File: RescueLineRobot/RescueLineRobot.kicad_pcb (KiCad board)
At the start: 2 copper layers, 100 x 100 mm, 8 parts, among them J1 Conn_01x11, J2 Bateria, J3 Motor 1, J4 Motor 2, J5 Convertidor, U1 ROB-14450, U2 ESP32-DEVKIT-V1

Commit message: updates
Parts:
- added J6: Laser 1, Connector_JST:JST_XH_B4B-XH-A_1x04_P2.50mm_Vertical, F.Cu at (168.0, 56.2)
- added J7: Laser 2, Connector_JST:JST_XH_B4B-XH-A_1x04_P2.50mm_Vertical, F.Cu at (168.0, 64.0)
- added J8: Laser 3, Connector_JST:JST_XH_B4B-XH-A_1x04_P2.50mm_Vertical, F.Cu at (168.0, 72.5)
- moved J4 7.52 mm to (170.0, 98.5)
- moved J3 6.77 mm to (228.8, 99.0)
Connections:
- U2 pad 11: unconnected-(U2-D21-Pad11) -> Net-(J6-Pin_4)
- U2 pad 14: unconnected-(U2-D22-Pad14) -> Net-(J6-Pin_3)
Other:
- board size 100 x 100 mm -> 80 x 100 mm

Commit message: Motores funcionan :D
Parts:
- moved U1 27.4 mm to (185.4, 90.2)
- moved J1 26.5 mm to (234.4, 70.0), turned to -90 degrees
- moved J3 17.8 mm to (219.8, 114.3)
- moved U2 15.6 mm to (215.9, 75.2)
- moved J4 9.51 mm to (168.9, 108.0)
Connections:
- U2 pad 10: Net-(U1-PWMA) -> Net-(U1-PWMB)
- U2 pad 26: Net-(U1-AI1) -> unconnected-(U2-D14-Pad26)
- U2 pad 28: Net-(U1-AI2) -> unconnected-(U2-D13-Pad28)
- U2 pad 5: Net-(U1-BI2) -> Net-(U1-PWMA)
- U2 pad 6: unconnected-(U2-RX2-Pad6) -> Net-(U1-AI2)
- U2 pad 7: unconnected-(U2-TX2-Pad7) -> Net-(U1-AI1)
- U2 pad 9: Net-(U1-PWMB) -> Net-(U1-BI2)

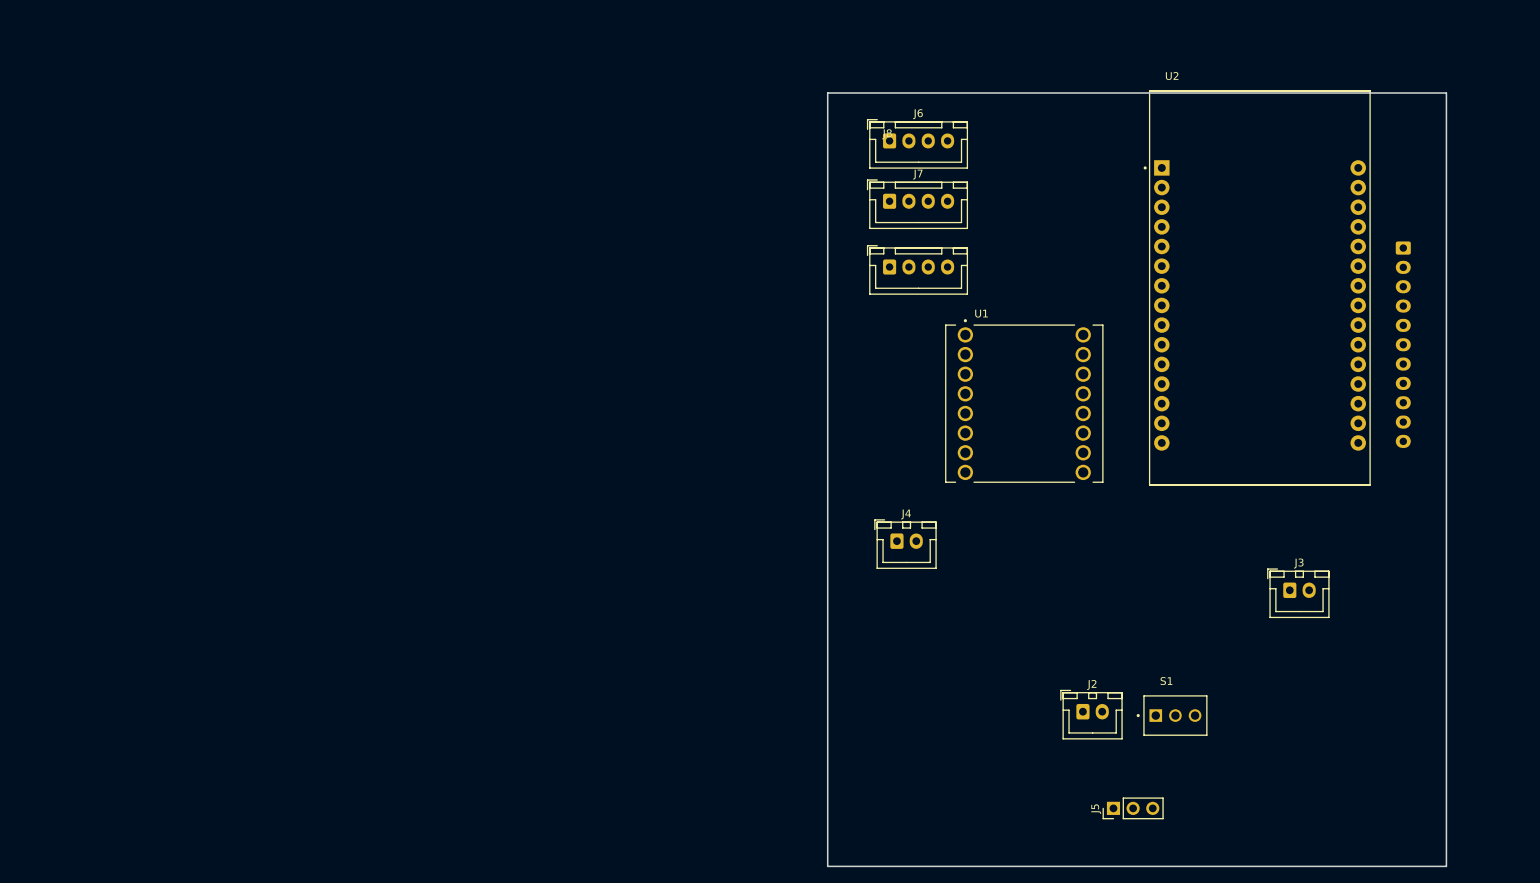
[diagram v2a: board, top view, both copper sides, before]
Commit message: Actualizacion de pcb
Ahora la pcb está más limpia y con serigrafía
Pendientes:
-2 Sensores RGB
-1 Botón pulsador
-2 Encoders para los motores (aun no se si cuadraticos o no)
-1 Puerto para servo (maybe con selector de voltaje)
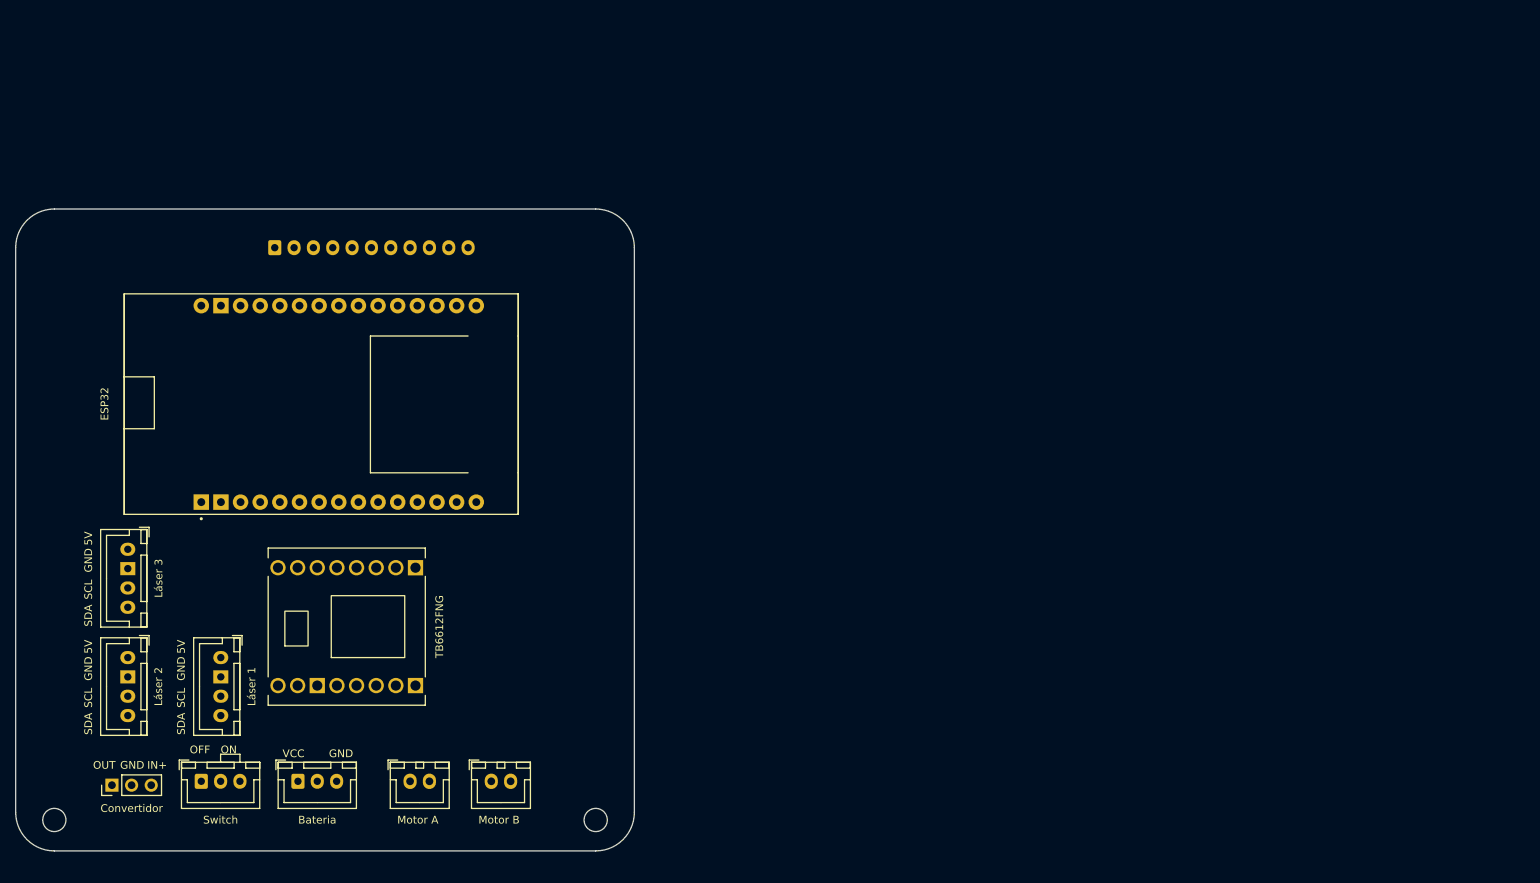
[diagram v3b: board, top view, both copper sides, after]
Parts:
- removed J2: Bateria, Connector_JST:JST_XH_B2B-XH-A_1x02_P2.50mm_Vertical
- removed J3: Motor 1, Connector_JST:JST_XH_B2B-XH-A_1x02_P2.50mm_Vertical
- removed J4: Motor 2, Connector_JST:JST_XH_B2B-XH-A_1x02_P2.50mm_Vertical
- removed J5: Convertidor, Connector_PinHeader_2.54mm:PinHeader_1x03_P2.54mm_Vertical
- removed S1: 200MSP1T2B4M2QE, 200MSP1T2B4M2QE:SW_200MSP1T2B4M2QE
- added Bateria: Bateria, Connector_JST:JST_XH_B3B-XH-A_1x03_P2.50mm_Vertical, F.Cu at (91.5, 139.0)
- added Convertidor: Convertidor, Connector_PinHeader_2.54mm:PinHeader_1x03_P2.54mm_Vertical, F.Cu at (67.5, 139.5)
- added Motor A: Motor 1, Connector_JST:JST_XH_B2B-XH-A_1x02_P2.50mm_Vertical, F.Cu at (106.0, 139.0)
- added Motor B: Motor 2, Connector_JST:JST_XH_B2B-XH-A_1x02_P2.50mm_Vertical, F.Cu at (116.5, 139.0)
- added Switch: Switch, Connector_JST:JST_XH_B3B-XH-A_1x03_P2.50mm_Vertical, F.Cu at (79.0, 139.0)
- Láser 1: renamed from J6
- Láser 2: renamed from J8
- Láser 3: renamed from J7
- moved J1 145.9 mm to (88.5, 70.0), turned to 0 degrees
- moved ESP32 122.3 mm to (94.5, 90.2), turned to 90 degrees
- moved Láser 2 110.7 mm to (69.5, 123.0), turned to -90 degrees
- moved Láser 1 109.3 mm to (81.5, 123.0), turned to -90 degrees
- moved Láser 3 108.3 mm to (69.5, 109.0), turned to -90 degrees
- moved TB6612FNG 92.2 mm to (97.8, 119.0), turned to 90 degrees
- renumbered U2 to ESP32, U1 to TB6612FNG
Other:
- board size 80 x 100 mm -> 80 x 83 mm
- board text added: "5V"
- board text added: "GND"
- board text added: "IN+"
- board text added: "OFF"
- board text added: "ON"
- board text added: "OUT"
- board text added: "SCL"
- board text added: "SDA"
- board text added: "VCC"

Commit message: Boton y encoders
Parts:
- added Boton1: SW_Push, Button_Switch_THT:SW_PUSH-12mm, F.Cu at (123.0, 124.8)
- added EncoderA1: Encoder A, Connector_JST:JST_XA_B03B-XASK-1_1x03_P2.50mm_Vertical, F.Cu at (106.0, 117.5)
- added EncoderB1: Encoder B, Connector_JST:JST_XA_B03B-XASK-1_1x03_P2.50mm_Vertical, F.Cu at (106.0, 131.5)
- added Resistencia1: R, Resistor_THT:R_Axial_DIN0617_L17.0mm_D6.0mm_P25.40mm_Horizontal, F.Cu at (106.7, 71.0)
- Laser1: renamed from Láser 1
- Laser2: renamed from Láser 3
- Laser3: renamed from Láser 2
- MotorA1: renamed from Motor A
- MotorB1: renamed from Motor B; value Motor 2 -> MotorB
- moved Laser1 30.9 mm to (69.5, 94.5)
- moved MotorA1 30.2 mm to (81.0, 122.0)
- moved MotorB1 30.2 mm to (91.5, 122.0)
- moved SigueLineas1 21.1 mm to (83.5, 49.5)
- moved Esp32 18.5 mm to (94.5, 71.7)
- moved TB6612FNG1 18.5 mm to (96.2, 100.6)
- renumbered Bateria to Bateria1, Convertidor to Convertidor1, ESP32 to Esp32, J1 to SigueLineas1, Switch to Switch1, TB6612FNG to TB6612FNG1
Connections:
- Esp32 pad 26: unconnected-(U2-D14-Pad26) -> Net-(EncoderB1-Pin_2)
- Esp32 pad 27: unconnected-(U2-D12-Pad27) -> Net-(Esp32-D12)
- Esp32 pad 28: unconnected-(U2-D13-Pad28) -> Net-(EncoderA1-Pin_2)
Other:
- board size 80 x 83 mm -> 80 x 103 mm

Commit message: Estamos Casi
Están todas las rutas hechas, todos los puertos necesarios, sólo falta nombrar al robot y poner gráficas
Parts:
- removed Convertidor1: Convertidor, Connector_PinHeader_2.54mm:PinHeader_1x03_P2.54mm_Vertical
- added Convertidor: Convertidor, Connector_PinHeader_2.54mm:PinHeader_1x03_P2.54mm_Vertical, F.Cu at (67.4, 139.0)
- added I2C1: ~, Connector_JST:JST_XH_B4B-XH-A_1x04_P2.50mm_Vertical, F.Cu at (128.3, 68.2)
- added I2C2: ~, Connector_JST:JST_XH_B4B-XH-A_1x04_P2.50mm_Vertical, F.Cu at (128.2, 53.0)
- added RGB1: ~, Connector_JST:JST_XH_B4B-XH-A_1x04_P2.50mm_Vertical, F.Cu at (128.5, 90.0)
- added RGB2: ~, Connector_JST:JST_XH_B4B-XH-A_1x04_P2.50mm_Vertical, F.Cu at (128.5, 104.6)
- added SERVO: Conn_01x03, Connector_JST:JST_XH_B3B-XH-A_1x03_P2.50mm_Vertical, F.Cu at (118.0, 106.0)
- added SERVOPOWER: Conn_01x03, Connector_PinHeader_1.27mm:PinHeader_1x03_P1.27mm_Vertical, F.Cu at (117.5, 95.2)
- EncoderA: renamed from EncoderA1; moved to B.Cu
- EncoderB: renamed from EncoderB1; moved to B.Cu
- MotorA: renamed from MotorA1; moved to B.Cu
- MotorB: renamed from MotorB1; moved to B.Cu
- moved Resistencia 24.7 mm to (82.5, 66.0), turned to 0 degrees
- moved SigueLineas 4.52 mm to (83.5, 45.0)
- moved Esp32 4.32 mm to (95.5, 67.5)
- moved Bateria 2.50 mm to (94.0, 139.0)
- moved Boton 2.50 mm to (125.5, 124.8)
- moved Switch 2.50 mm to (81.5, 139.0)
- moved EncoderA 1.50 mm to (107.5, 117.5)
- moved EncoderB 1.50 mm to (107.5, 131.5)
- moved MotorA 0.79 mm to (81.2, 122.8)
- moved MotorB 0.75 mm to (91.5, 122.8)
- renumbered Bateria1 to Bateria, Boton1 to Boton, Resistencia1 to Resistencia, SigueLineas1 to SigueLineas, Switch1 to Switch, TB6612FNG1 to TB6612FNG
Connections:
- net Net-(Bateria1-Pin_1) renamed VIN
- net Net-(Bateria1-Pin_3) renamed GND
- net Net-(Convertidor1-Pin_1) renamed 5V
- net Net-(Convertidor1-Pin_3) renamed 7V4
- net Net-(EncoderA1-Pin_2) renamed D13
- net Net-(Esp32-3V3) renamed 3V3
- net Net-(Esp32-D18) renamed D18
- net Net-(Esp32-D19) renamed D19
- net Net-(Esp32-D21) renamed D21
- net Net-(Esp32-D22) renamed D22
- net Net-(Esp32-D25) renamed D25
- net Net-(Esp32-D26) renamed D26
- net Net-(Esp32-D27) renamed D27
- net Net-(Esp32-D32) renamed D32
- net Net-(Esp32-D33) renamed D33
- net Net-(Esp32-D34) renamed D34
- net Net-(Esp32-D35) renamed D35
- net Net-(Esp32-D4) renamed D4
- net Net-(Esp32-D5) renamed D5
- net Net-(Esp32-RX2) renamed D16
- net Net-(Esp32-TX2) renamed D17
- net Net-(Esp32-VN) renamed D39
- net Net-(Esp32-VP) renamed D36
- Boton pad 1: Net-(Esp32-D12) -> D12
- EncoderB pad 2: Net-(EncoderB1-Pin_2) -> D14
- Esp32 pad 15: unconnected-(Esp32-D23-Pad15) -> D23
- Esp32 pad 26: Net-(EncoderB1-Pin_2) -> D12
- Esp32 pad 27: Net-(Esp32-D12) -> unconnected-(Esp32-D12-Pad27)
- Esp32 pad 3: unconnected-(Esp32-D15-Pad3) -> D14
- Resistencia pad 2: Net-(Esp32-D12) -> D12
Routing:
- net GND: track 0.00 -> 491.4 mm, vias 0 -> 2
- net 5V: track 0.00 -> 387.5 mm
- net D21: track 0.00 -> 193.4 mm, vias 0 -> 1
- net D22: track 0.00 -> 179.1 mm, vias 0 -> 4
- net D13: track 0.00 -> 104.6 mm, vias 0 -> 1
- net D12: track 0.00 -> 95.7 mm, vias 0 -> 2
- net 7V4: track 0.00 -> 85.3 mm
- net D14: track 0.00 -> 81.4 mm, vias 0 -> 1
- net 3V3: track 0.00 -> 56.7 mm
- net D23: track 0.00 -> 38.2 mm, vias 0 -> 2
- net Net-(MotorA1-Pin_1): track 0.00 -> 21.1 mm
- net Net-(MotorA1-Pin_2): track 0.00 -> 19.7 mm
- net ServoV: track 0.00 -> 19.3 mm
- net Net-(MotorB1-Pin_2): track 0.00 -> 17.3 mm
- net Net-(MotorB1-Pin_1): track 0.00 -> 17.3 mm
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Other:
- board size 80 x 103 mm -> 80 x 110 mm
- board text added: "7V4"
- board text added: "D13"
- board text added: "D14"
- board text added: "D23"
- board text added: "Diseñado en Chile Programa de Ciencia y Tecnología Fundación Gabriel y Mary Mustakis"
- board text added: "VIN"

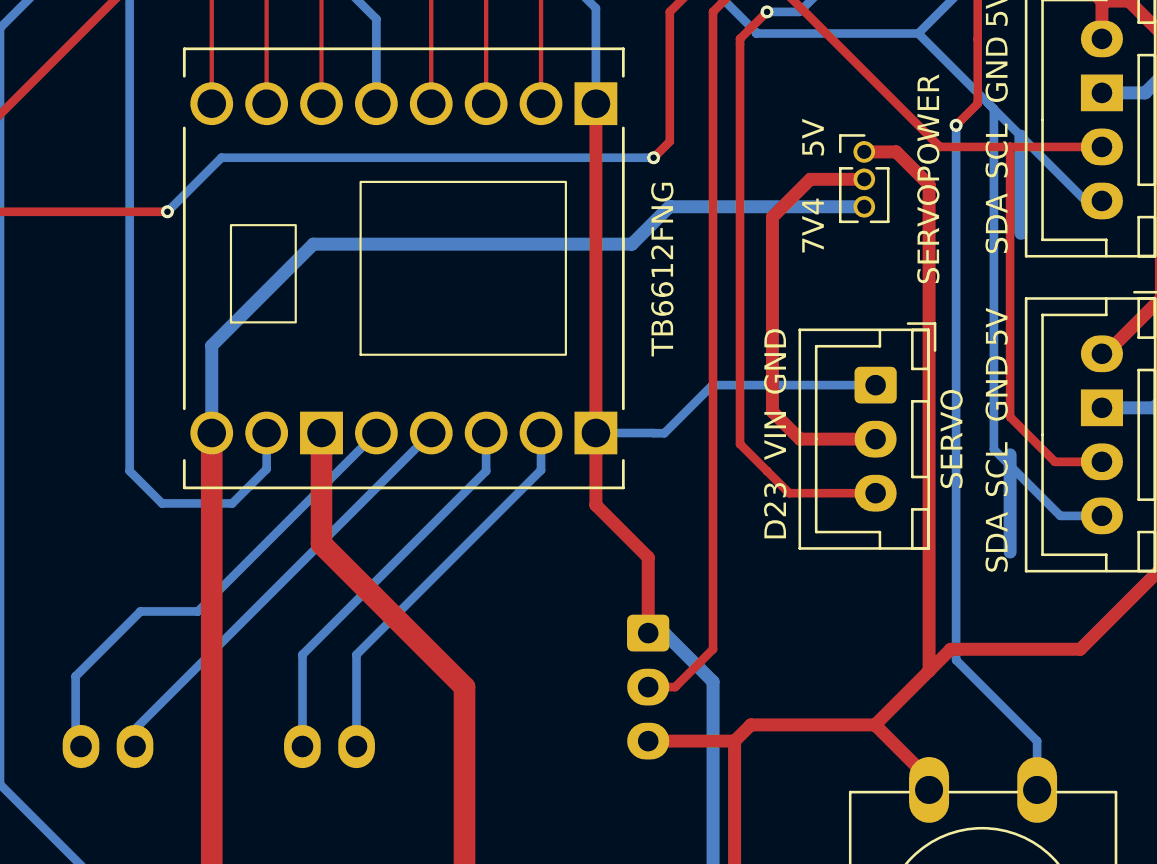
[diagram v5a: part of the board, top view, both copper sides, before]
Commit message: logo update
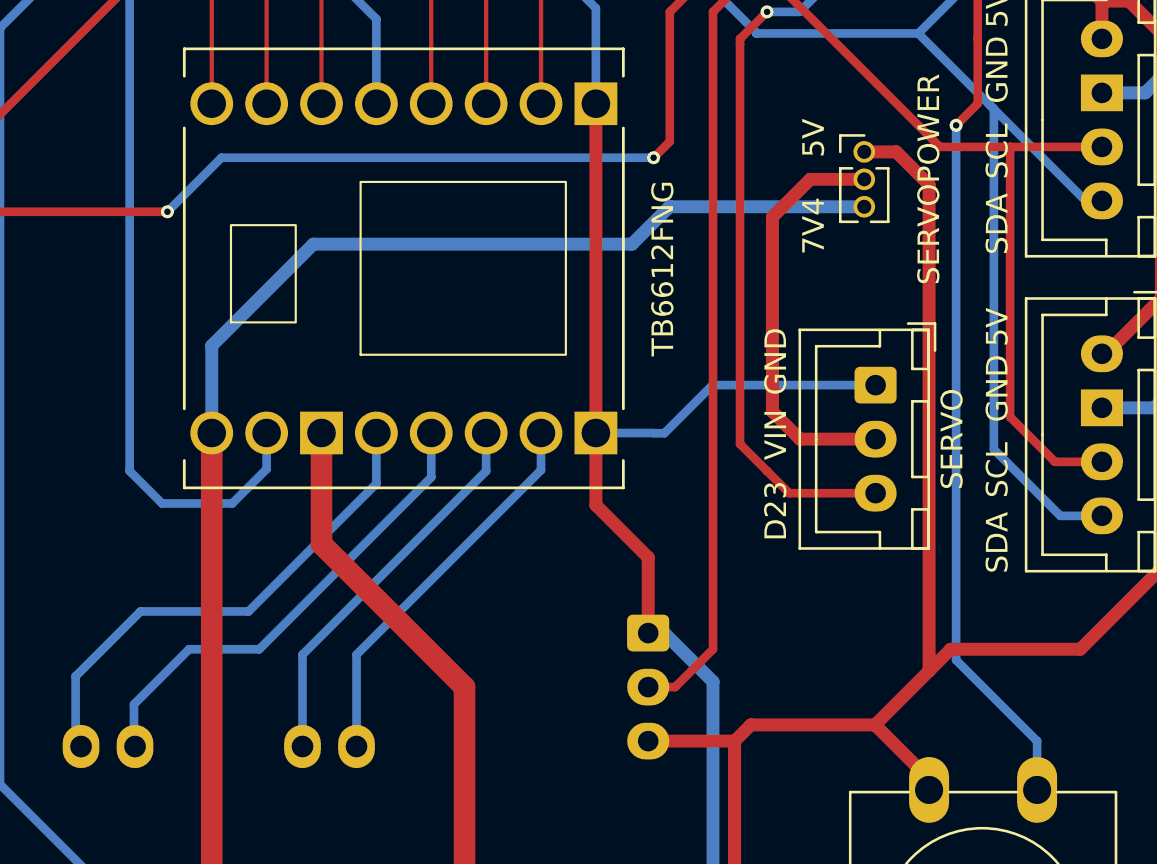
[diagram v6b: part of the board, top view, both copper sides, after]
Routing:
- net D21: track 193.4 -> 184.4 mm
- net Net-(MotorA1-Pin_2): track 19.7 -> 21.6 mm
- net Net-(MotorA1-Pin_1): track 21.1 -> 22.5 mm
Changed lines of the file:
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@@
 		)
 		(property "Value" "R"
-			(at 12.7 4.12 360)
+			(at 12.7 4.12 0)
 			(layer "F.Fab")
 			(effects
@@
 		)
 		(fp_text user "${REFERENCE}"
-			(at 12.7 0 360)
+			(at 12.7 0 0)
 			(layer "F.Fab")
 			(effects
@@
 		)
 		(property "Value" "Convertidor"
-			(at 0 7.41 270)
+			(at 0 7.41 -90)
 			(layer "F.Fab")
 			(effects
@@
 		)
 		(fp_text user "${REFERENCE}"
-			(at 0 2.54 360)
+			(at 0 2.54 0)
 			(layer "F.Fab")
 			(effects
@@
 		(at 96.19 100.62 90)
 		(property "Reference" "TB6612FNG"
-			(at 0 12 270)
+			(at 0 12 -90)
 			(layer "F.SilkS")
 			(effects
@@
 		)
 		(property "Value" "Motor 1"
-			(at 1.25 -4.6 360)
+			(at 1.25 -4.6 0)
 			(layer "B.Fab")
 			(hide yes)
@@
 		)
 		(property "Value" "MotorB"
-			(at 1.25 -4.6 360)
+			(at 1.25 -4.6 0)
 			(layer "B.Fab")
 			(hide yes)
@@
 		(layer "F.SilkS")
 	)
+	(gr_poly
+		(pts
+			(xy 84.25 128.223126) (xy 80.678126 128.223126) (xy 80.678126 124.651251) (xy 84.25 124.651251)
+		)
+		(stroke
+			(width -0.000001)
+			(type solid)
+		)
+		(fill solid)
+		(layer "Dwgs.User")
+	)
+	(gr_poly
+		(pts
+			(xy 91.453281 121) (xy 87.881407 121) (xy 87.881407 117.428126) (xy 91.453281 117.428126)
+		)
+		(stroke
+			(width -0.000001)
+			(type solid)
+		)
+		(fill solid)
+		(layer "Dwgs.User")
+	)
+	(gr_poly
+		(pts
+			(xy 105.879686 128.223126) (xy 102.30781 128.223126) (xy 102.30781 117.408282) (xy 105.879686 117.408282)
+		)
+		(stroke
+			(width -0.000001)
+			(type solid)
+		)
+		(fill solid)
+		(layer "Dwgs.User")
+	)
+	(gr_poly
+		(pts
+			(xy 84.25 121) (xy 80.678126 121) (xy 80.678126 117.428126) (xy 84.25 117.428126)
+		)
+		(stroke
+			(width -0.000001)
+			(type solid)
+		)
+		(fill solid)
+		(layer "Dwgs.User")
+	)
+	(gr_poly
+		(pts
+			(xy 98.676407 128.223126) (xy 95.104531 128.223126) (xy 95.104531 117.408282) (xy 98.676407 117.408282)
+		)
+		(stroke
+			(width -0.000001)
+			(type solid)
+		)
+		(fill solid)
+		(layer "Dwgs.User")
+	)
+	(gr_poly
+		(pts
+			(xy 91.453281 128.223126) (xy 87.881407 128.223126) (xy 87.881407 124.651251) (xy 91.453281 124.651251)
+		)
+		(stroke
+			(width -0.000001)
+			(type solid)
+		)
+		(fill solid)
+		(layer "Dwgs.User")
+	)
 	(gr_circle
 		(center 130 145)
@@
 	)
 	(segment
-		(start 124.75 99)
-		(end 124.75 94.5)
-		(width 0.6)
-		(layer "B.Cu")
-		(net 5)
-	)
-	(segment
 		(start 120 89.75)
 		(end 123.25 93)
@@
 	)
 	(segment
-		(start 124.25 113.75)
-		(end 124.25 109.25)
-		(width 0.6)
-		(layer "B.Cu")
-		(net 5)
-	)
-	(segment
 		(start 123.25 93)
 		(end 123.5 93.25)
@@
 	)
 	(segment
+		(start 84 116.5)
+		(end 81 119.5)
+		(width 0.4)
+		(layer "B.Cu")
+		(net 7)
+	)
+	(segment
 		(start 81 119.5)
 		(end 81 122)
@@
 	)
 	(segment
-		(start 84 116.5)
-		(end 81 119.5)
+		(start 89 116.5)
+		(end 84 116.5)
 		(width 0.4)
 		(layer "B.Cu")
@@
 	)
 	(segment
-		(start 86.66 116.5)
-		(end 84 116.5)
+		(start 94.92 110.58)
+		(end 89 116.5)
 		(width 0.4)
 		(layer "B.Cu")
@@
 	(segment
 		(start 94.92 108.24)
-		(end 86.66 116.5)
+		(end 94.92 110.58)
 		(width 0.4)
 		(layer "B.Cu")
@@
 	)
 	(segment
+		(start 97.46 110.29)
+		(end 89.5 118.25)
+		(width 0.4)
+		(layer "B.Cu")
+		(net 8)
+	)
+	(segment
+		(start 86.25 118.25)
+		(end 83.7 120.8)
+		(width 0.4)
+		(layer "B.Cu")
+		(net 8)
+	)
+	(segment
 		(start 97.46 108.24)
+		(end 97.46 110.29)
+		(width 0.4)
+		(layer "B.Cu")
+		(net 8)
+	)
+	(segment
+		(start 83.7 120.8)
 		(end 83.7 122)
 		(width 0.4)
@@
 	)
 	(segment
+		(start 89.5 118.25)
+		(end 86.25 118.25)
+		(width 0.4)
+		(layer "B.Cu")
+		(net 8)
+	)
+	(segment
 		(start 102.54 109.96)
 		(end 94 118.5)
@@
 		(net 38)
 	)
+	(group ""
+		(members "07bfc493-631f-4fb8-b22d-72fbf2ebc91d" "0e2ecd14-35b5-4a2c-b0a9-f50f017872c6"
+			"0ee545d9-85ef-4a35-8aa2-17c1312670f1" "373a8dcd-9351-4c16-b616-4588c93b46ba"
+			"af5ca039-081f-49c4-839f-0242b4c7638d" "c887cd54-4894-4a41-8eae-27cb9f6f41c2"
+		)
+	)
 )

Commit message: Dynamis a nacido
Estamos listos señores!!!
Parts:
- renumbered MotorA to MotorA1, MotorB to MotorB1, Resistencia to Resistencia1
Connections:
- Esp32 pad 26: D12 -> D14
- Esp32 pad 27: unconnected-(Esp32-D12-Pad27) -> D12
- Esp32 pad 3: D14 -> unconnected-(Esp32-D15-Pad3)
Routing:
- net D14: track 81.4 -> 111.4 mm
- net GND: track 491.4 -> 489.4 mm
- net D12: track 95.7 -> 96.0 mm, vias 2 -> 3
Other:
- board text added: "Diseñado en Chile Programa de Ciencia y Tecnología Fundación Gabriel & Mary Mustakis"
- board text added: "Dynamis Bot, 2024"
- board text removed: "Diseñado en Chile Programa de Ciencia y Tecnología Fundación Gabriel y Mary Mustakis"
